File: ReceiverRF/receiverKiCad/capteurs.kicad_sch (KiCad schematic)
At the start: 11 parts, among them J1 RF2-03E-T-00-50-G, J3 Conn_01x04, U4 MLX90393SLW-ABA-011-RE

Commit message: changement vers footprint 1206
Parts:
- MLX_C1, MLX_C2: footprint Capacitor_SMD:C_0402_1005Metric -> Capacitor_SMD:C_1206_3216Metric
- MLX_C3: footprint Capacitor_SMD:C_0603_1608Metric -> Capacitor_SMD:C_1206_3216Metric
- MLX_R1, MLX_R2: footprint Resistor_SMD:R_0402_1005Metric -> Resistor_SMD:R_1206_3216Metric
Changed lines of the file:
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@@
 			)
 		)
-		(property "Footprint" "Resistor_SMD:R_0402_1005Metric"
+		(property "Footprint" "Resistor_SMD:R_1206_3216Metric"
 			(at 97.282 71.12 90)
 			(effects
@@
 			)
 		)
-		(property "Footprint" "Resistor_SMD:R_0402_1005Metric"
+		(property "Footprint" "Resistor_SMD:R_1206_3216Metric"
 			(at 108.712 68.58 90)
 			(effects
@@
 			)
 		)
-		(property "Footprint" "Capacitor_SMD:C_0402_1005Metric"
+		(property "Footprint" "Capacitor_SMD:C_1206_3216Metric"
 			(at 103.8352 39.37 0)
 			(effects
@@
 			)
 		)
-		(property "Footprint" "Capacitor_SMD:C_0402_1005Metric"
+		(property "Footprint" "Capacitor_SMD:C_1206_3216Metric"
 			(at 47.9552 39.37 0)
 			(effects
@@
 			)
 		)
-		(property "Footprint" "Capacitor_SMD:C_0603_1608Metric"
+		(property "Footprint" "Capacitor_SMD:C_1206_3216Metric"
 			(at 86.0552 39.37 0)
 			(effects

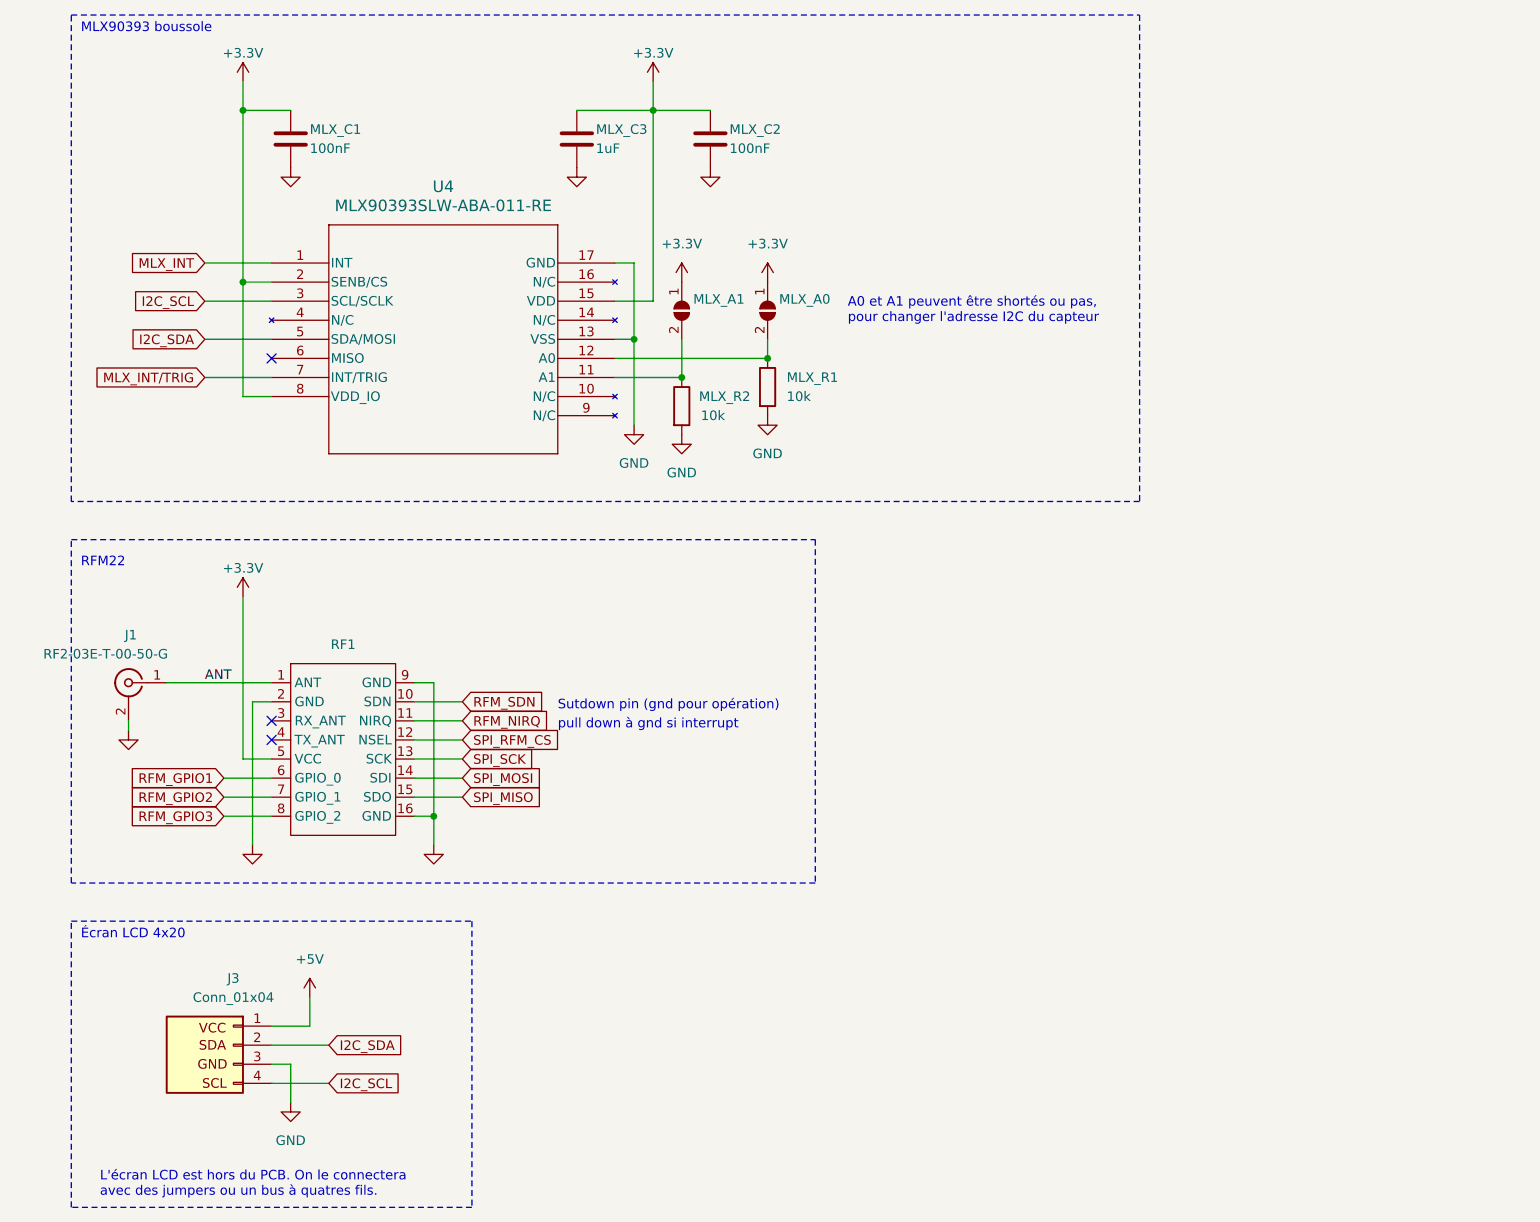
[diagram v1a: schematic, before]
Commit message: changement BOM et choix nouvelles pièces 1206
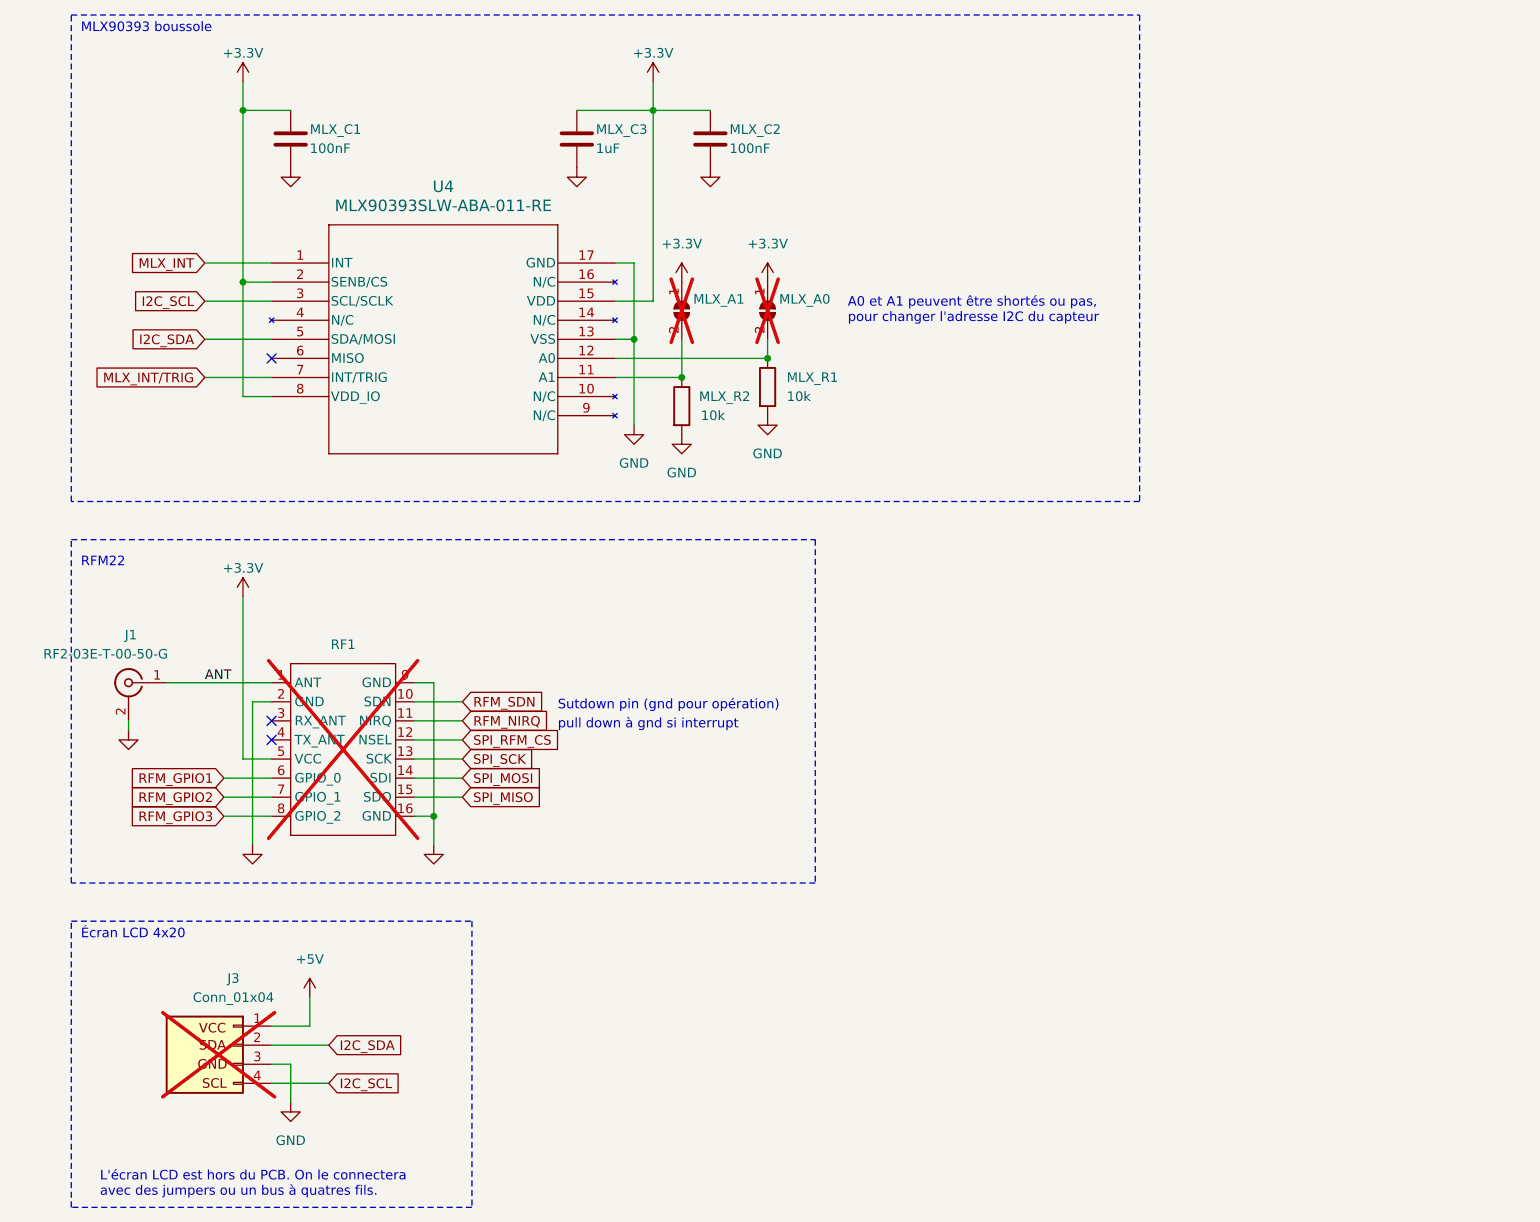
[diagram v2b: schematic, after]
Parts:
- J3, MLX_A0, MLX_A1: now not fitted
- MLX_C1, MLX_C2: Digikey 2679-AGC0402X7R500-104KNPTR-ND -> 399-C1206C104K5RACTUCT-ND
- MLX_C3: Digikey 2679-AGC0603X7R250-105KXPTR-ND -> 1276-1068-1-ND
- MLX_R1, MLX_R2: Digikey 311-10KJRCT-ND -> 311-10.0KFRCT-ND
- RF1: Digikey BAT54T1GOSCT-ND -> (none); now not fitted
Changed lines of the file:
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@@
 			)
 		)
-		(property "Digikey" "311-10KJRCT-ND"
+		(property "Digikey" "311-10.0KFRCT-ND"
 			(at 99.06 71.12 0)
 			(effects
@@
 		(in_bom yes)
 		(on_board yes)
-		(dnp no)
+		(dnp yes)
 		(property "Reference" "MLX_A0"
 			(at 112.014 56.896 90)
@@
 			)
 		)
-		(property "Digikey" "311-10KJRCT-ND"
+		(property "Digikey" "311-10.0KFRCT-ND"
 			(at 110.49 68.58 0)
 			(effects
@@
 			)
 		)
-		(property "Digikey" "2679-AGC0402X7R500-104KNPTR-ND"
+		(property "Digikey" "399-C1206C104K5RACTUCT-ND"
 			(at 102.87 35.56 0)
 			(effects
@@
 		(in_bom yes)
 		(on_board yes)
-		(dnp no)
+		(dnp yes)
 		(fields_autoplaced yes)
 		(property "Reference" "RF1"
@@
 			)
 		)
-		(property "Digikey" "BAT54T1GOSCT-ND"
+		(property "Digikey" ""
 			(at 54.61 107.95 0)
 			(effects
@@
 			)
 		)
-		(property "Digikey" "2679-AGC0402X7R500-104KNPTR-ND"
+		(property "Digikey" "399-C1206C104K5RACTUCT-ND"
 			(at 46.99 35.56 0)
 			(effects
@@
 			)
 		)
-		(property "Digikey" "  2679-AGC0603X7R250-105KXPTR-ND"
+		(property "Digikey" "1276-1068-1-ND"
 			(at 85.09 35.56 0)
 			(effects
@@
 		(in_bom yes)
 		(on_board yes)
-		(dnp no)
+		(dnp yes)
 		(property "Reference" "MLX_A1"
 			(at 100.584 56.896 90)
@@
 		(in_bom yes)
 		(on_board yes)
-		(dnp no)
+		(dnp yes)
 		(fields_autoplaced yes)
 		(property "Reference" "J3"

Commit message: ideFIX v2 fix schematic, layout
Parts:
- removed J3: Conn_01x04, Connector_PinHeader_2.00mm:PinHeader_1x04_P2.00mm_Vertical, symbol Connector_Generic:Conn_01x04
- added D2, D3, D4: LTST-C170GKT, Footprints:LTST-C170GKT, symbol Device:LED
- added LED_R1, LED_R2, LED_R3: 145R, Resistor_SMD:R_1206_3216Metric, symbol Device:R
- MLX_A0, MLX_A1: now fitted
- RF1: footprint Footprints:RFM22b-S2 -> Footprints:RFM22b-S2_TH
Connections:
- net GND: now also D2.1 (K), D3.1 (K), D4.1 (K)
- net RFM_GPIO4: now reaches RF1.3 (RX_ANT)
- net RFM_GPIO5: now reaches RF1.4 (TX_ANT)
- new net: D4.2 (A), LED_R3.2
- new net: D2.2 (A), LED_R1.2
- new net: D3.2 (A), LED_R2.2
- new net LED1: LED_R1.1
- new net LED2: LED_R2.1
- new net LED3: LED_R3.1
- no-connect marks 3 -> 1
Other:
- note added: "Ces LED tirent 10mA chacunes"
- note added: "LED d'état"
- note removed: "L'écran LCD est hors du PCB. On le connectera avec des jumpers ou un bus à quatres fils."
- note removed: "Écran LCD 4x20"
- moved on the sheet: J1, RF1

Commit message: revision schematic before tracing
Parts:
- RF1: value BAT54T1G -> RFM22B; now fitted
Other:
- company: (none) -> GAUL
- title: (none) -> IdeFIX
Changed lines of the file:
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@@
 	(generator_version "8.0")
 	(paper "A4")
+	(title_block
+		(title "IdeFIX")
+		(rev "v2")
+		(company "GAUL")
+	)
 	(junction
 		(at 92.71 62.23)
@@
 		(in_bom yes)
 		(on_board yes)
-		(dnp yes)
+		(dnp no)
 		(fields_autoplaced yes)
 		(property "Reference" "RF1"
@@
 			)
 		)
-		(property "Value" "BAT54T1G"
+		(property "Value" "RFM22B"
 			(at 53.34 106.68 0)
 			(effects

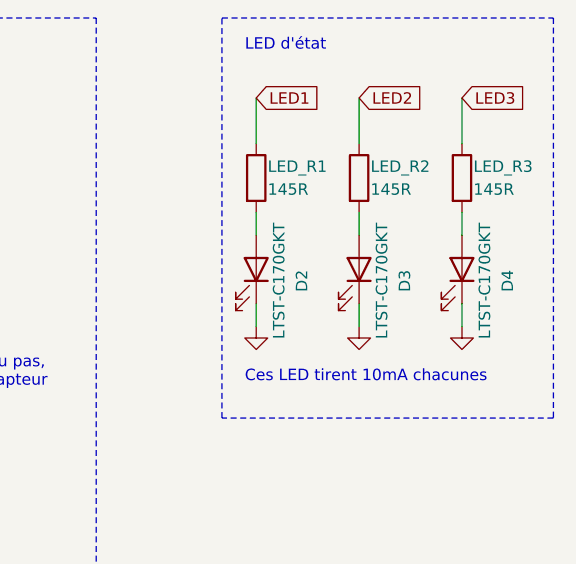
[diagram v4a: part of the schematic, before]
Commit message: fix zener diode footprint, thermal relief on SMA conn, more work on silkscreen
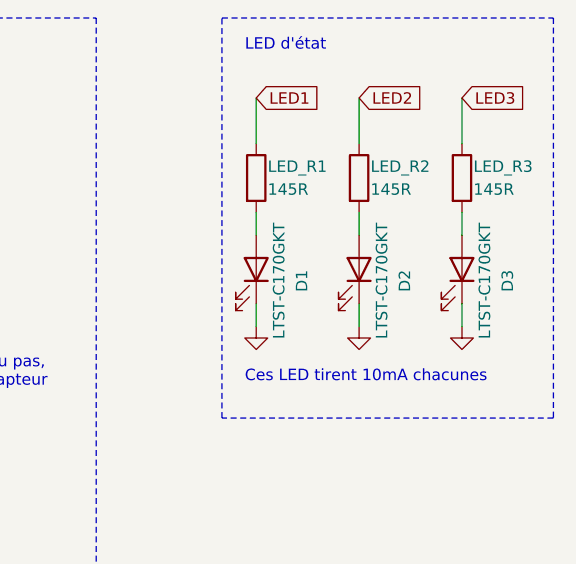
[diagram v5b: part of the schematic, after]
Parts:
- renumbered D2 to D1, D3 to D2, D4 to D3
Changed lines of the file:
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@@
 		(on_board yes)
 		(dnp no)
-		(property "Reference" "D4"
+		(property "Reference" "D3"
 			(at 205.74 48.26 0)
 			(effects
@@
 			(project "receiver"
 				(path "/439ba515-58d4-4b14-87ab-b438dcf423a5/56b56711-4d65-4df6-9470-6736a83e438d"
-					(reference "D4")
+					(reference "D3")
 					(unit 1)
 				)
@@
 		(on_board yes)
 		(dnp no)
-		(property "Reference" "D2"
+		(property "Reference" "D1"
 			(at 182.88 48.26 0)
 			(effects
@@
 			(project "receiver"
 				(path "/439ba515-58d4-4b14-87ab-b438dcf423a5/56b56711-4d65-4df6-9470-6736a83e438d"
-					(reference "D2")
+					(reference "D1")
 					(unit 1)
 				)
@@
 		(on_board yes)
 		(dnp no)
-		(property "Reference" "D3"
+		(property "Reference" "D2"
 			(at 194.31 48.26 0)
 			(effects
@@
 			(project "receiver"
 				(path "/439ba515-58d4-4b14-87ab-b438dcf423a5/56b56711-4d65-4df6-9470-6736a83e438d"
-					(reference "D3")
-					(unit 1)
-				)
+					(reference "D2")
+					(unit 1)
+				)

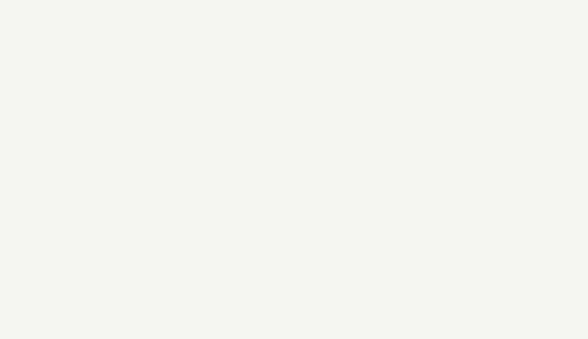
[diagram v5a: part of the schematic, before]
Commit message: 3.2mm holes, XT30 connector, add polyfuse, minor fixes
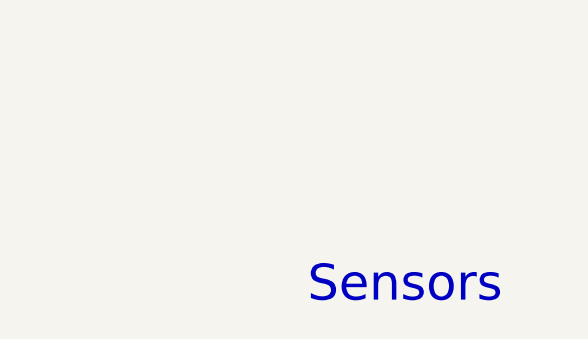
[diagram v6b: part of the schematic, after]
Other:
- note added: "Sensors"
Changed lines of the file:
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@@
+		)
+	)
+	(text "Sensors"
+		(exclude_from_sim no)
+		(at 193.04 172.974 0)
+		(effects
+			(font
+				(size 4 4)
+			)
 		)
 	)

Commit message: Refactor timer handling and add TRANSMIT/RECEIVE definition macros
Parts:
- D1, D2, D3: Digikey 160-1179-1-ND -> 160-1414-1-ND
- RF1: now left out of the parts list
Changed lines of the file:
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@@
 			)
 		)
-		(property "Description" ""
+		(property "Description" "10k Res"
 			(at 99.06 71.12 0)
 			(effects
@@
 			)
 		)
-		(property "Datasheet" "https://www.digikey.ca/en/products/detail/liteon/LTST-C170GKT/269226"
+		(property "Datasheet" "https://www.digikey.ca/en/products/detail/liteon/LTST-C170KGKT/386776"
 			(at 200.66 46.99 0)
 			(effects
@@
 			)
 		)
-		(property "Description" ""
+		(property "Description" "Green led"
 			(at 200.66 46.99 0)
 			(effects
@@
 			)
 		)
-		(property "Digikey" "160-1179-1-ND"
+		(property "Digikey" "160-1414-1-ND"
 			(at 200.66 46.99 0)
 			(effects
@@
 			)
 		)
-		(property "Datasheet" "https://www.digikey.ca/en/products/detail/liteon/LTST-C170GKT/269226"
+		(property "Datasheet" "https://www.digikey.ca/en/products/detail/liteon/LTST-C170KGKT/386776"
 			(at 177.8 46.99 0)
 			(effects
@@
 			)
 		)
-		(property "Description" ""
+		(property "Description" "Green led"
 			(at 177.8 46.99 0)
 			(effects
@@
 			)
 		)
-		(property "Digikey" "160-1179-1-ND"
+		(property "Digikey" "160-1414-1-ND"
 			(at 177.8 46.99 0)
 			(effects
@@
 			)
 		)
-		(property "Description" ""
+		(property "Description" "145o Res"
 			(at 200.66 36.83 0)
 			(effects
@@
 			)
 		)
-		(property "Description" ""
+		(property "Description" "10k Res"
 			(at 110.49 68.58 0)
 			(effects
@@
 			)
 		)
-		(property "Description" ""
+		(property "Description" "100nF Cap"
 			(at 102.87 35.56 0)
 			(effects
@@
 			)
 		)
-		(property "Description" ""
+		(property "Description" "145o Res"
 			(at 189.23 36.83 0)
 			(effects
@@
 			)
 		)
-		(property "Datasheet" "MLX90393SLW-ABA-011-RE"
+		(property "Datasheet" "https://www.digikey.ca/en/products/detail/melexis-technologies-nv/MLX90393SLW-ABA-011-RE/5031683?s=N4IgTCBcDaILIBkAaBOADAZhRgygg6gLQCCAQsYWgIxWEBKAogMIAqhAcgCIgC6AvkA"
 			(at 36.83 46.99 0)
 			(effects
@@
 			)
 		)
-		(property "Description" ""
+		(property "Description" "Magnetometer"
 			(at 44.45 52.07 0)
 			(effects
@@
 			)
 		)
-		(property "Description" ""
+		(property "Description" "145o Res"
 			(at 177.8 36.83 0)
 			(effects
@@
 		(unit 1)
 		(exclude_from_sim no)
-		(in_bom yes)
+		(in_bom no)
 		(on_board yes)
 		(dnp no)
@@
 			)
 		)
-		(property "Description" ""
+		(property "Description" "100nF Cap"
 			(at 46.99 35.56 0)
 			(effects
@@
 			)
 		)
-		(property "Description" ""
+		(property "Description" "1uF Cap"
 			(at 85.09 35.56 0)
 			(effects
@@
 			)
 		)
-		(property "Datasheet" "https://www.digikey.ca/en/products/detail/liteon/LTST-C170GKT/269226"
+		(property "Datasheet" "https://www.digikey.ca/en/products/detail/liteon/LTST-C170KGKT/386776"
 			(at 189.23 46.99 0)
 			(effects
@@
 			)
 		)
-		(property "Description" ""
+		(property "Description" "Green led"
 			(at 189.23 46.99 0)
 			(effects
@@
 			)
 		)
-		(property "Digikey" "160-1179-1-ND"
+		(property "Digikey" "160-1414-1-ND"
 			(at 189.23 46.99 0)
 			(effects
@@
 			)
 		)
-		(property "Description" ""
+		(property "Description" "SMA connector"
 			(at 24.13 107.95 0)
 			(effects
